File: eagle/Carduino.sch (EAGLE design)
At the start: 88 parts, among them IC11 RV-3028-C7_32.768KHZ_1PPM_TA_Q, IC2 FT232RL, IC3 SN74HCS596DR, IC4 SN74HCS596DR, IC5 SN74HCS596DR, IC6 SN74HCS596DR, IC7 NTMD4184PFR2G, IC8 ATTINY404-SSNR, IC9 MCP73831T-3ACI_OT, U1 BAT-HLD-012-SMT

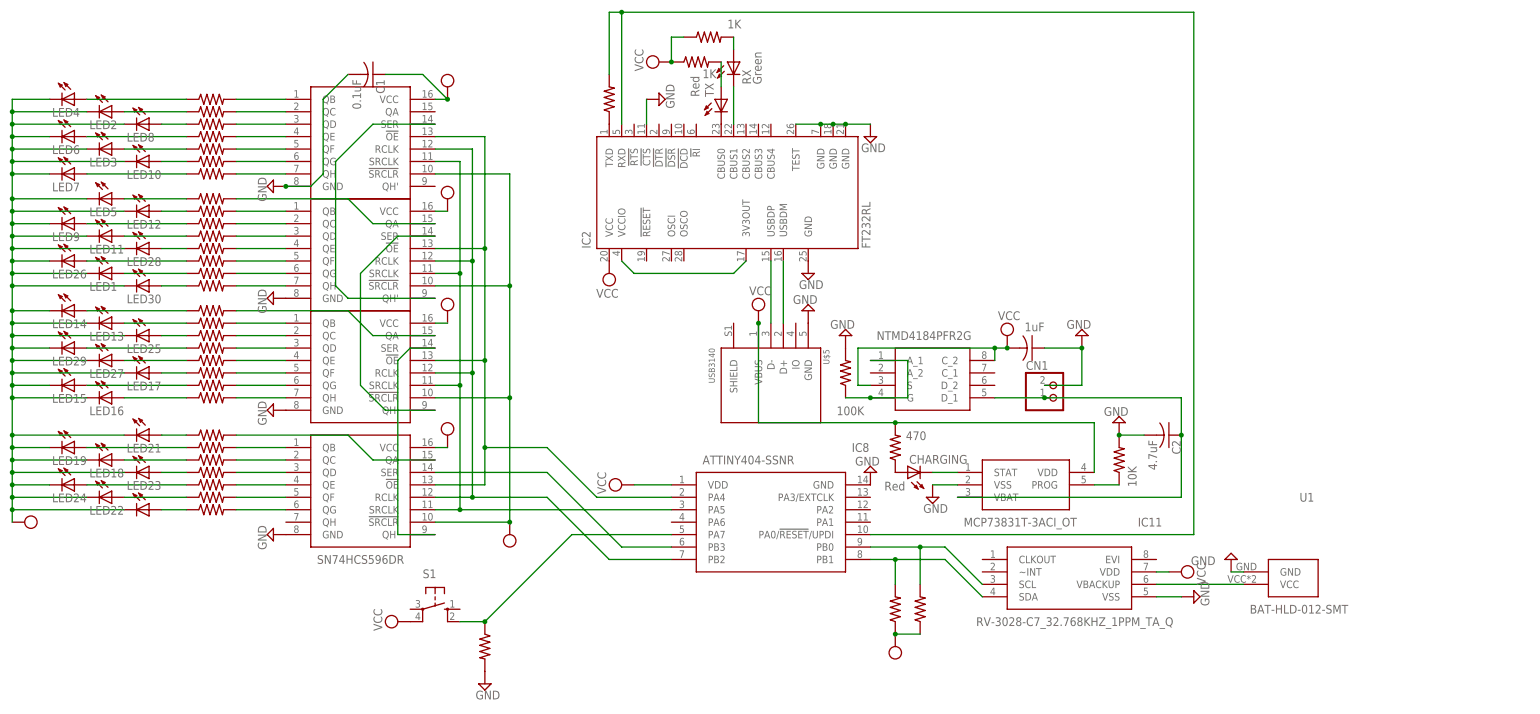
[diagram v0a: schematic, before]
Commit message: swaping ftdi chip with CP2102N
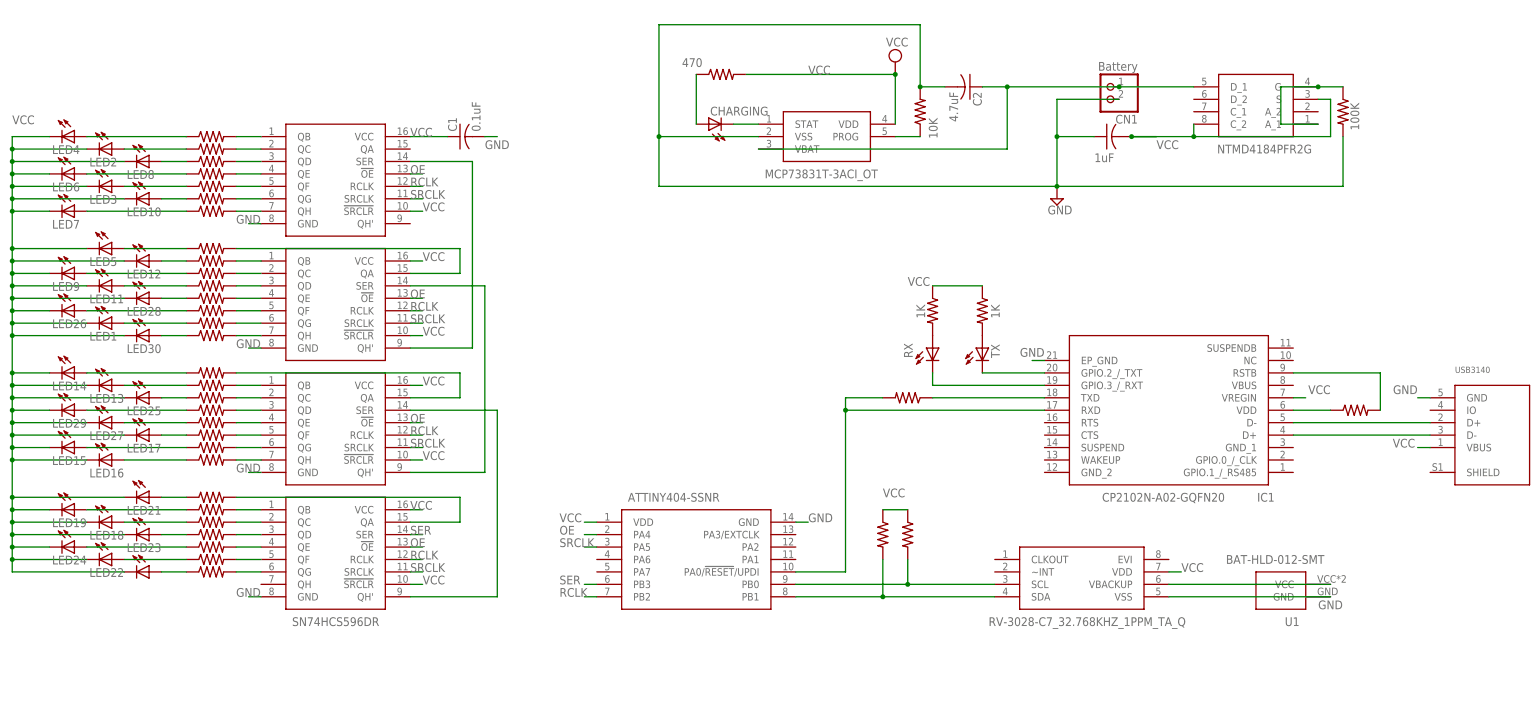
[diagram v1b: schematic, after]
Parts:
- removed IC2: FT232RL, ftdichip:FT232RL
- removed R6: 4.7K, adafruit:R-US_R0805
- removed S1: (no value), adafruit:40-XX-ROUND
- added IC1: CP2102N-A02-GQFN20, SamacSys_Parts:CP2102N-A02-GQFN20
- added R23: 1K, adafruit:R-US_R0805
- CN1: value (none) -> Battery
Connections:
- net N$35 renamed OE
- net N$96 renamed SRCLK
- net N$97 renamed RCLK
- net N$98 renamed SER
- removed net N$101: IC2.3V3OUT, IC2.VCCIO
- removed net N$102: IC2.TXD, R1.1
- removed net N$106: IC2.CBUS0, TX.C
- removed net N$107: IC2.CBUS1, RX.C
- removed net N$34: IC8.PA7, R6.1, S1.S1
- new net N$41: IC1.GPIO.2_/_TXT, TX.C
- new net N$42: IC1.GPIO.3_/_RXT, RX.C
- new net N$43: IC1.TXD, R1.1
- new net N$44: IC1.VDD, R23.1
- new net N$45: IC1.RSTB, R23.2
- net GND: now also IC1.EP_GND; no longer IC2.!CTS, IC2.GND, IC2.GND@1, IC2.GND@2, IC2.GND@A, IC2.TEST, R6.2
- net N$100: now also IC1.D+; no longer IC2.USBDP
- net N$103: now also IC1.RXD; no longer IC2.RXD
- net N$99: now also IC1.D-; no longer IC2.USBDM
- net VCC: now also IC1.VREGIN; no longer IC2.VCC, S1.P1
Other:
- note added: "LEDs and drivers"
- note added: "Load sharing battery charging"
- note added: "MCU, USB and RTC"
- moved on the sheet: C1, C2, CHARGING, CN1, LED1, LED10, LED11, LED12, LED13, LED14, LED15, LED16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
